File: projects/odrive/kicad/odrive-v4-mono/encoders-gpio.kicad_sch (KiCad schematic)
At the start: 55 parts, among them J10 ENC_M1_JST-GH, J11 ENC_SPI_JST-GH, J12 GPIO_2x4, J9 ENC_M0_JST-GH, U30 TPS2553DBV, U31 TPS2553DBV, U35 SN74LVC2G17, U36 SN74LVC2G17, U37 SN74LVC2G17, U38 TPD4E05U06, U39 TPD4E05U06, U40 SN74LVC1G125, U41 TPD4E05U06, U42 TPD1E10B06

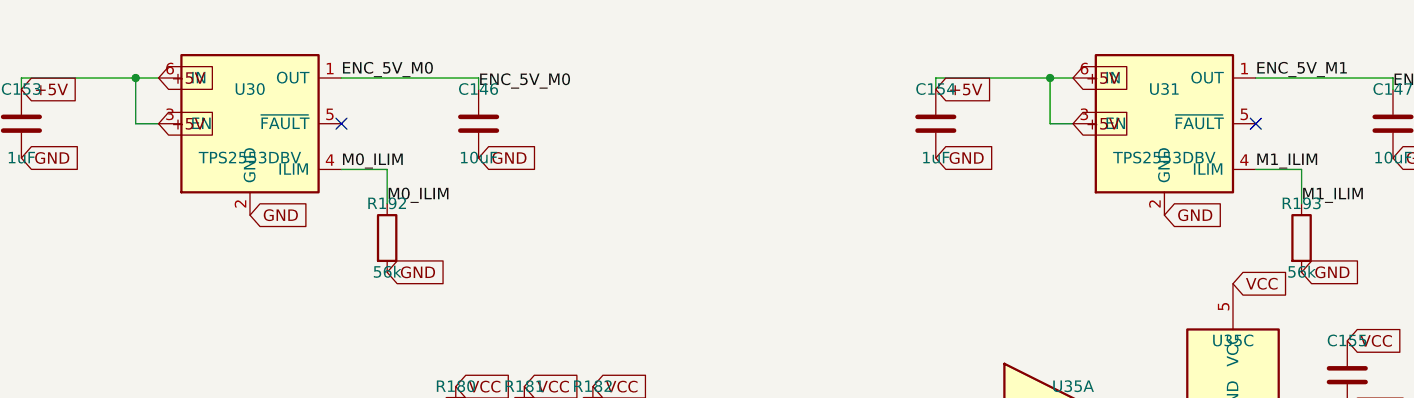
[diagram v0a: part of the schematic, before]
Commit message: Checkpoint ODrive 56 V recovery and modular handoff
Preserve corrected schematics, local libraries, partial PCB routing, firmware diagnostics, analysis tools and the independent modular-study handoff. The board remains incomplete with 381 unconnected items and 415 DRC warnings.

Validation: 52 host tests, ARM component compilation, schematic/PCB parity, native copper preservation, DRC, STEP export, Python lint, shellcheck and nix fmt. Known Konnect-generated schematic whitespace is retained. No fabrication or hardware validation is claimed.
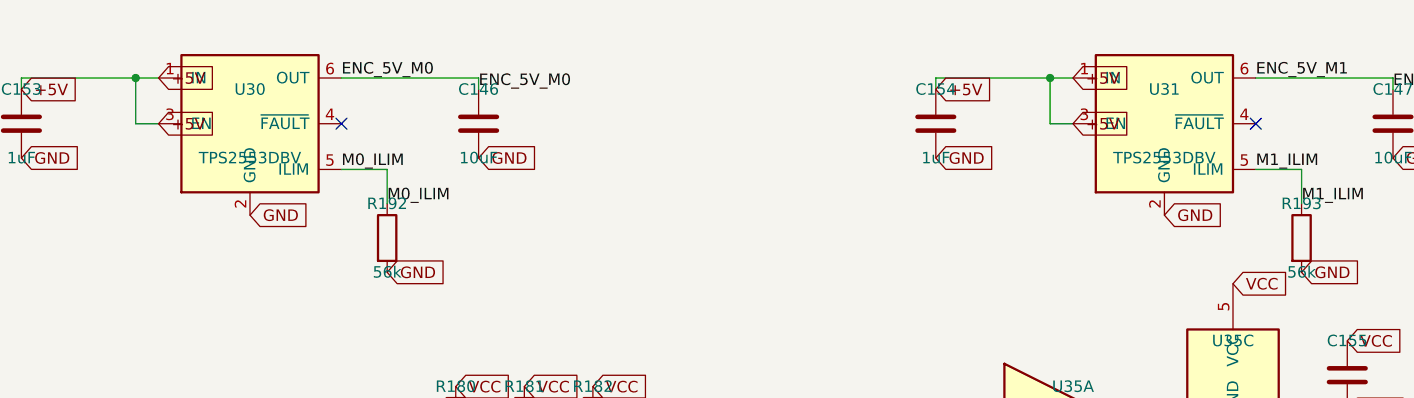
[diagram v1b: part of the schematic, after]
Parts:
- U30, U31: symbol /home/aldo/Dev/aldoborrero/cad/.claude/worktrees/odrive/projects/odrive/kicad/odrive-v4/odrive-v4-symbols:TPS2553DBV -> odrive-mono:TPS2553DBV; MPN (none) -> TPS2553DBVR; Manufacturer (none) -> Texas Instruments
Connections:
- net +5V: now also U30.1 (IN), U31.1 (IN); no longer U30.6 (IN), U31.6 (IN)
- net ENC_5V_M0: now also U30.6 (OUT); no longer U30.1 (OUT)
- net ENC_5V_M1: now also U31.6 (OUT); no longer U31.1 (OUT)
- net M0_ILIM: now also U30.5 (ILIM); no longer U30.4 (ILIM)
- net M1_ILIM: now also U31.5 (ILIM); no longer U31.4 (ILIM)
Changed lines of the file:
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@@
   )
   (symbol
-    (lib_id "/home/aldo/Dev/aldoborrero/cad/.claude/worktrees/odrive/projects/odrive/kicad/odrive-v4/odrive-v4-symbols:TPS2553DBV")
+    (lib_id "odrive-mono:TPS2553DBV")
     (at 63.5 50.8 0)
     (unit 1)
@@
       )
     )
-    (property "Datasheet" ""
+    (property "Datasheet" "https://www.ti.com/lit/ds/symlink/tps2553.pdf"
       (at 63.5 50.8 0)
       (hide yes)
@@
       )
     )
-  )
+    (property "MPN" "TPS2553DBVR"
+    	(at 63.5 50.8 0)
+    	(hide yes)
+    	(effects
+    		(font
+    			(size 1.27 1.27)
+    		)
+    	)
+    )
+    (property "Manufacturer" "Texas Instruments"
+    	(at 63.5 50.8 0)
+    	(hide yes)
+    	(effects
+    		(font
+    			(size 1.27 1.27)
+    		)
+    	)
+    ))
   (symbol
-    (lib_id "/home/aldo/Dev/aldoborrero/cad/.claude/worktrees/odrive/projects/odrive/kicad/odrive-v4/odrive-v4-symbols:TPS2553DBV")
+    (lib_id "odrive-mono:TPS2553DBV")
     (at 165.1 50.8 0)
     (unit 1)
@@
       )
     )
-    (property "Datasheet" ""
+    (property "Datasheet" "https://www.ti.com/lit/ds/symlink/tps2553.pdf"
       (at 165.1 50.8 0)
       (hide yes)
@@
       )
     )
-  )
+    (property "MPN" "TPS2553DBVR"
+    	(at 165.1 50.8 0)
+    	(hide yes)
+    	(effects
+    		(font
+    			(size 1.27 1.27)
+    		)
+    	)
+    )
+    (property "Manufacturer" "Texas Instruments"
+    	(at 165.1 50.8 0)
+    	(hide yes)
+    	(effects
+    		(font
+    			(size 1.27 1.27)
+    		)
+    	)
+    ))
   (symbol
     (lib_id "/home/aldo/Dev/aldoborrero/cad/.claude/worktrees/odrive/projects/odrive/kicad/odrive-v4/odrive-v4-symbols:TPD1E10B06")
